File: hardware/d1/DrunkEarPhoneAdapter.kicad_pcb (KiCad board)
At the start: 4 copper layers, 50 x 35 mm, 185 parts, among them J3 SWD, J4 UART, Q1 CSD17577Q3A, Q2 CSD17577Q3A, Q3 DMG1012T-7, SW1 SSSS811101, SW2 DSHP04TS-S, U1 CS43131-CNZR, U10 BLM15PX601SN1D, U11 TPS7A2033PDBVR, U12 TPS7A2018PDBVR, U13 TPS7A2018PDBVR, U14 BLM15PX601SN1D, U15 ESDA25P35-1U1M, U16 ESDA25P35-1U1M, U17 SN74LVC1G32DBVR, U18 TPS22917DBVR, U19 TPS22917DBVR, U2 STM32G0B1VCT6, U20 SN74AVC4T774RSVR, U21 TCA9406DCUR, U3 TS3USB221RSER, U4 TCPP03-M20, U5 TCPP03-M20, U6 ES8327, U7 TPS7A2018PDBVR, U8 TPS7A2033PDBVR, U9 TPS560430XFDBVR, X1 22.5792MHz, X3 24.576MHz

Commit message: Fix Caps
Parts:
- removed C53, C55: 4.7uF 10V X5R, JLCImport:CL05A475MP5NRNC
- added C2: 4.7uF 10V X5R, Capacitor_SMD:C_0603_1608Metric, F.Cu at (66.9, 124.2)
- added C3: 4.7uF 10V X5R, Capacitor_SMD:C_0603_1608Metric, F.Cu at (60.5, 130.9)
- added C85: 1uF 25V X5R, JLCImport:CL05A105KA5NQNC, F.Cu at (70.3, 124.0)
- added JP2: SolderJumper_2_Bridged, Jumper:SolderJumper-2_P1.3mm_Bridged_RoundedPad1.0x1.5mm, F.Cu at (60.7, 118.8)
- added JP3: SolderJumper_2_Bridged, Jumper:SolderJumper-2_P1.3mm_Bridged_RoundedPad1.0x1.5mm, F.Cu at (60.7, 122.3)
- added JP4: SolderJumper_2_Bridged, Jumper:SolderJumper-2_P1.3mm_Bridged_RoundedPad1.0x1.5mm, F.Cu at (60.7, 125.9)
- added R43: 100kΩ, JLCImport:0402WGF1003TCE, F.Cu at (70.4, 128.5)
- C16, C7: footprint JLCImport:CL05A475MP5NRNC -> Capacitor_SMD:C_0603_1608Metric
- C31, C32: value 2.2uF 16V X5R -> 2.2uF 50V X7R; footprint JLCImport:CL05A225KO5NQNC -> JLCImport:CC0805KKX7R9BB225
- moved C7 58.0 mm to (66.9, 128.7)
- moved C16 47.8 mm to (66.9, 131.2)
- moved C31 16.3 mm to (67.4, 118.5)
- moved C32 16.2 mm to (67.4, 121.4)
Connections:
- C16 pad 1: Net-(U1-VP) -> GND
- C16 pad 2: GND -> +3V3_D
- C32 pad 1: GND -> /dac/VCP_FILT-
- C32 pad 2: /dac/VCP_FILT- -> GND
- C66 pad 1: /ucpd/GDPs -> /ucpd/USB_PHONE_ISENSE
- C7 pad 2: +1V8_D -> +3V3_D
- U4 pad 8: unconnected-(U4-GDCs-Pad8) -> /ucpd/GDCs
- U5 pad 6: unconnected-(U5-GDPs-Pad6) -> /ucpd/GDPs_CHR
- U5 pad 8: unconnected-(U5-GDCs-Pad8) -> /ucpd/GDCs_CHR

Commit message: Fixes
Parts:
- removed R43: 100kΩ, JLCImport:0402WGF1003TCE
- added R26: 47kΩ, Resistor_SMD:R_0402_1005Metric, F.Cu at (45.5, 61.5)
- R19, R20: value 510Ω -> 549Ω
- moved R19 25.6 mm to (40.0, 61.8)
- moved R20 25.6 mm to (40.0, 64.3)
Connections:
- R42 pad 2: /ucpd/USB_DIR -> /mcu/USB_DIR
- SW1 pad 1: GND -> unconnected-(SW1-Pad1)
- U3 pad 9: /ucpd/USB_DIR -> /mcu/USB_DIR

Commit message: Replace parts
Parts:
- removed C34: 2.2uF 16V X5R, JLCImport:CL05A225KO5NQNC
- removed C44, C50, C52: 100nF 16V X7R, JLCImport:CL05B104KO5NNNC
- removed C70, C71, C72, C73: 330pF 50V, Capacitor_SMD:C_0402_1005Metric
- removed C80, C81, C82, C83: 1nF 50V X7R, Capacitor_SMD:C_0402_1005Metric
- removed R40, R41: 10kΩ 0603, Resistor_SMD:R_0603_1608Metric
- added C100: 100nF 50V, Capacitor_SMD:C_0402_1005Metric, F.Cu at (46.6, 162.4)
- added C101: 100nF 50V, Capacitor_SMD:C_0402_1005Metric, F.Cu at (41.7, 135.0)
- added C102: 100nF 50V, Capacitor_SMD:C_0402_1005Metric, F.Cu at (41.7, 137.0)
- added C103: 100nF 50V, Capacitor_SMD:C_0402_1005Metric, F.Cu at (41.7, 138.9)
- added C104: 100nF 50V, Capacitor_SMD:C_0402_1005Metric, F.Cu at (41.7, 140.9)
- added C105: 100nF 50V, Capacitor_SMD:C_0402_1005Metric, F.Cu at (31.9, 160.7)
- added C106: 100nF 50V, Capacitor_SMD:C_0402_1005Metric, F.Cu at (46.6, 164.4)
- added C53: 100nF 50V, Capacitor_SMD:C_0402_1005Metric, F.Cu at (35.9, 135.0)
- added C55: 100nF 50V, Capacitor_SMD:C_0402_1005Metric, F.Cu at (35.9, 137.0)
- added C95: 100nF 50V, Capacitor_SMD:C_0402_1005Metric, F.Cu at (31.9, 154.8)
- added C96: 100nF 50V, Capacitor_SMD:C_0402_1005Metric, F.Cu at (31.9, 156.8)
- added C97: 100nF 50V, Capacitor_SMD:C_0402_1005Metric, F.Cu at (46.6, 160.5)
- added C98: 100nF 50V, Capacitor_SMD:C_0402_1005Metric, F.Cu at (38.8, 140.9)
- added C99: 100nF 50V, Capacitor_SMD:C_0402_1005Metric, F.Cu at (31.9, 158.8)
- added R27: 33Ω, Resistor_SMD:R_0402_1005Metric, F.Cu at (36.0, 144.9)
- added R43: 33Ω, Resistor_SMD:R_0402_1005Metric, F.Cu at (36.0, 148.8)
- added R44: 33Ω, Resistor_SMD:R_0402_1005Metric, F.Cu at (36.0, 150.8)
- C1, C19, C20, C21, C22: value 100nF 16V X7R -> 1nF 50V; footprint JLCImport:CL05B104KO5NNNC -> Capacitor_SMD:C_0402_1005Metric
- C13: value 4.7uF 10V X5R -> 2.2uF 16V; footprint JLCImport:CL05A475MP5NRNC -> Capacitor_SMD:C_0603_1608Metric
- C16, C2, C3, C7: value 4.7uF 10V X5R -> 2.2uF 16V
- C23, C24, C35, C37, C39, C40: value 100nF 16V X7R -> 4.7uF 16V; footprint JLCImport:CL05B104KO5NNNC -> Capacitor_SMD:C_0603_1608Metric
- C25: value 2.2uF 16V X5R -> 2.2uF 16V; footprint JLCImport:CL05A225KO5NQNC -> Capacitor_SMD:C_0603_1608Metric
- C26, C27: value 15uF 35V X5R -> 22uF 25V X5R; footprint JLCImport:C2012X5R1V156MT000E -> JLCImport:CL21A226MAQNNNE
- C28, C29, C30, C33: value 2.2uF 16V X5R -> 330pF 50V; footprint JLCImport:CL05A225KO5NQNC -> Capacitor_SMD:C_0603_1608Metric
- C54, C56, C69, C74, C77, C78, C79, C84, C89, C90, C91, C92: value 100nF 16V X7R -> 100nF 50V; footprint JLCImport:CL05B104KO5NNNC -> Capacitor_SMD:C_0402_1005Metric
- C86, C87, C88: value 100nF 50V X7R -> 100nF 50V
- R16, R9: value 33Ω -> 1kΩ
- R23: value 0Ω -> 1kΩ
- R30: value 0Ω -> 10kΩ; footprint Resistor_SMD:R_0402_1005Metric -> Resistor_SMD:R_0603_1608Metric
- R35: value 1kΩ -> 10kΩ; footprint Resistor_SMD:R_0402_1005Metric -> Resistor_SMD:R_0603_1608Metric
- moved R38 154.6 mm to (36.0, 146.9)
- moved R16 147.1 mm to (50.6, 146.8)
- moved C69 144.7 mm to (46.6, 158.5)
- moved C56 123.3 mm to (46.6, 156.5)
- moved C35 93.2 mm to (37.4, 155.1)
- moved C40 93.0 mm to (37.4, 157.6)
- moved C39 89.4 mm to (50.0, 157.3)
- moved C86 84.9 mm to (40.8, 156.8)
- moved C37 84.1 mm to (50.0, 154.8)
- moved C87 69.0 mm to (53.4, 140.9)
- moved C88 69.0 mm to (53.4, 142.9)
- moved C89 67.9 mm to (35.9, 140.9)
- moved C13 67.6 mm to (32.5, 142.8)
- moved C84 67.2 mm to (53.4, 138.9)
- moved C90 62.6 mm to (38.8, 135.0)
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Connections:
- C1 pad 1: Net-(U9-CB) -> unconnected-(C1-Pad1)
- C1 pad 2: Net-(U9-SW) -> unconnected-(C1-Pad2)
- C13 pad 1: GND -> +1V8_CP
- C13 pad 2: +1V8_CP -> GND
- C16 pad 1: GND -> /dac/FLYP_VCP
- C16 pad 2: +3V3_D -> /dac/FLYC_VCP
- C19 pad 1: Net-(U18-QOD) -> GND
- C19 pad 2: GND -> /mcu/ADC1_IN0
- C2 pad 2: Net-(U1-VP) -> +1V8_A
- C20 pad 1: Net-(U2-VREF+) -> GND
- C20 pad 2: GND -> /mcu/ADC1_IN1
- C21 pad 2: Net-(U1-VP) -> /mcu/ADC1_IN2
- C22 pad 1: Net-(U1-VD) -> GND
- C22 pad 2: GND -> /mcu/ADC1_IN3
- C23 pad 1: GND -> unconnected-(C23-Pad1)
- C23 pad 2: +1V8_A -> unconnected-(C23-Pad2)
- C24 pad 1: Net-(U1-VD) -> GND
- C24 pad 2: GND -> Net-(U1-VP)
- C25 pad 1: +1V8_A -> /dac/FLYC_VCP
- C25 pad 2: GND -> /dac/FLYN_VCP
- C27 pad 1: /dac/-VA -> /dac/FILT-
- C27 pad 2: /dac/FILT- -> /dac/-VA
- C28 pad 1: /dac/-VA -> GND
- C28 pad 2: GND -> /ucpd/USB_CHR_CC1
- C29 pad 1: /dac/FLYP_VA -> GND
- C29 pad 2: /dac/FLYN_VA -> /ucpd/USB_CHR_CC2
- C3 pad 1: GND -> /dac/-VA
- C3 pad 2: +1V8_D -> GND
- C30 pad 1: +1V8_CP -> GND
- C30 pad 2: GND -> /ucpd/USB_PHONE_CC1
- C33 pad 1: /dac/FLYP_VCP -> GND
- C33 pad 2: /dac/FLYC_VCP -> /ucpd/USB_PHONE_CC2
- C35 pad 1: Net-(U6-AVDD) -> GND
- C35 pad 2: GND -> +1V8_D
- C37 pad 1: Net-(U6-CPVDD) -> GND
- C37 pad 2: GND -> +3V3_D
- C39 pad 1: +3V3_D -> GND
- C39 pad 2: GND -> +3V3_D
- C40 pad 1: +3V3_D -> GND
- C40 pad 2: GND -> +1V8_CP
- C54 pad 1: +3V3_D -> GND
- C54 pad 2: GND -> +3V3_D
- C56 pad 1: GND -> /mcu/NRST
- C56 pad 2: /mcu/NRST -> GND
- C69 pad 1: +3V3_D -> GND
- C69 pad 2: GND -> +3V3_D
- C7 pad 1: GND -> /dac/FLYN_VA
- C7 pad 2: +3V3_D -> /dac/FLYP_VA
- C74 pad 1: +3V3_D -> GND
- C74 pad 2: GND -> +3V3_D
- C78 pad 1: Net-(U17-VCC) -> GND
- C78 pad 2: GND -> +3V3_D
- C79 pad 1: Net-(U17-VCC) -> Net-(U9-CB)
- C79 pad 2: GND -> Net-(U9-SW)
- C84 pad 1: +3V3_D -> GND
- C84 pad 2: GND -> +3V3_D
- C88 pad 1: GND -> Net-(U5-CBIAS)
- C88 pad 2: Net-(U5-CBIAS) -> GND
- C89 pad 1: GND -> +1V8_D
- C89 pad 2: +1V8_D -> GND
- C90 pad 1: +3V3_D -> GND
- C90 pad 2: GND -> +3V3_D
- C91 pad 1: GND -> +3V3_D
- C91 pad 2: +3V3_D -> GND
- C92 pad 1: GND -> +1V8_D
- C92 pad 2: +1V8_D -> GND
- R16 pad 1: Net-(U17-Y) -> /mcu/ADC1_IN2
- R16 pad 2: Net-(U1-XTI/MCLK) -> Net-(U5-IANA)
- R23 pad 1: /mcu/ADC1_IN0 -> Net-(U1-HP_DETECT)
- R23 pad 2: Net-(U4-IANA) -> /dac/JACK_TIP_DETECT
- R30 pad 1: /mcu/ADC1_IN2 -> /ucpd/VSENSE_PHONE
- R30 pad 2: Net-(U5-IANA) -> /ucpd/USB_PHONE_VBUS
- R35 pad 1: Net-(U1-HP_DETECT) -> /ucpd/VSENSE_CHR
- R35 pad 2: /dac/JACK_TIP_DETECT -> /ucpd/USB_CHR_VBUS
- R9 pad 1: Net-(U20-B3) -> /mcu/ADC1_IN0
- R9 pad 2: /adc/CLKIN -> Net-(U4-IANA)

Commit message: Trace
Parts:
- removed C1: 1nF 50V, Capacitor_SMD:C_0402_1005Metric
- removed C23: 4.7uF 16V, Capacitor_SMD:C_0603_1608Metric
- removed NT1: NetTie_2, NetTie:NetTie-2_SMD_Pad0.5mm
- removed R17: 10mΩ 500mW, Resistor_SMD:R_0805_2012Metric
- removed USBC2: ~, JLCImport:USBC_EXT_5P
- added NT3: NetTie_3, NetTie:NetTie-3_SMD_Pad0.5mm, F.Cu at (63.2, 44.7)
- added USBC3: ~, JLCImport:USBC_EXT_5P, F.Cu at (44.9, 36.7)
- added USBC4: ~, JLCImport:USBC_EXT_5P, B.Cu at (44.9, 36.7)
- C101, C102, C103, C104, C13, C2, C24, C85, L3, R23: moved to B.Cu
- R27: value 33Ω -> 7mΩ 500mW; footprint Resistor_SMD:R_0402_1005Metric -> Resistor_SMD:R_0805_2012Metric
- moved C40 227.3 mm to (252.1, 82.9)
- moved D2 224.6 mm to (272.3, 135.2)
- moved R1 224.6 mm to (270.4, 148.6)
- moved C51 221.8 mm to (265.7, 132.9)
- moved C57 221.8 mm to (265.7, 136.3)
- moved C58 221.8 mm to (265.7, 139.7)
- moved C59 221.8 mm to (265.7, 143.0)
- moved C60 221.8 mm to (265.7, 146.3)
- moved C9 221.8 mm to (265.7, 129.6)
- moved C15 204.0 mm to (252.1, 76.9)
- moved U13 204.0 mm to (256.5, 85.9)
- moved U7 199.5 mm to (223.6, 79.5)
- moved C35 197.0 mm to (221.7, 85.5)
- moved TP3 191.6 mm to (256.6, 78.7)
- moved C14 177.3 mm to (225.4, 82.9)
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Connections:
- Audio1 pad 4: GND -> /headset/JACK_RING_2
- D4 pad 4: /dac/JACK_TIP_DETECT -> /adc/GMS1
- D4 pad 5: /adc/GMS1 -> /dac/JACK_TIP_DETECT
- L7 pad 5: Net-(USBC2-D-) -> /ucpd/D_P
- L7 pad 6: Net-(USBC2-D+) -> /ucpd/D_N
- NT2 pad 2: GND -> /headset/JACK_RING_2
- R27 pad 1: unconnected-(R27-Pad1) -> /ucpd/USB_CHR_VBUS
- R27 pad 2: unconnected-(R27-Pad2) -> /ucpd/USB_CHR_ISENSE
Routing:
- net GND: track 0.00 -> 33.8 mm, vias 0 -> 145
- net /adc/GMS1: track 0.00 -> 29.7 mm, vias 0 -> 2
- net /adc/GMS0: track 0.00 -> 28.2 mm
- net /dac/HPREFA: track 0.00 -> 18.3 mm
- net +3V8: track 0.00 -> 15.6 mm, vias 0 -> 36
- net /adc/MIC1P: track 0.00 -> 13.1 mm, vias 0 -> 2
- net /dac/JACK_TIP_DETECT: track 0.00 -> 12.6 mm, vias 0 -> 1
- net /dac/JACK_RING_1: track 0.00 -> 11.8 mm
- net /dac/FLYN_VCP: track 0.00 -> 11.7 mm
- net /dac/JACK_TIP: track 0.00 -> 10.9 mm
- net /adc/MIC1N: track 0.00 -> 10.9 mm, vias 0 -> 2
- net /dac/HPREFB: track 0.00 -> 10.0 mm
- net /ucpd/USB_CHR_DP: track 0.00 -> 9.03 mm, vias 0 -> 2
- net /ucpd/USB_CHR_DN: track 0.00 -> 8.58 mm, vias 0 -> 2
- net /ucpd/USB_CHR_VBUS: track 0.00 -> 7.59 mm, vias 0 -> 4
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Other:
- board size 50 x 35 mm -> 50 x 45 mm

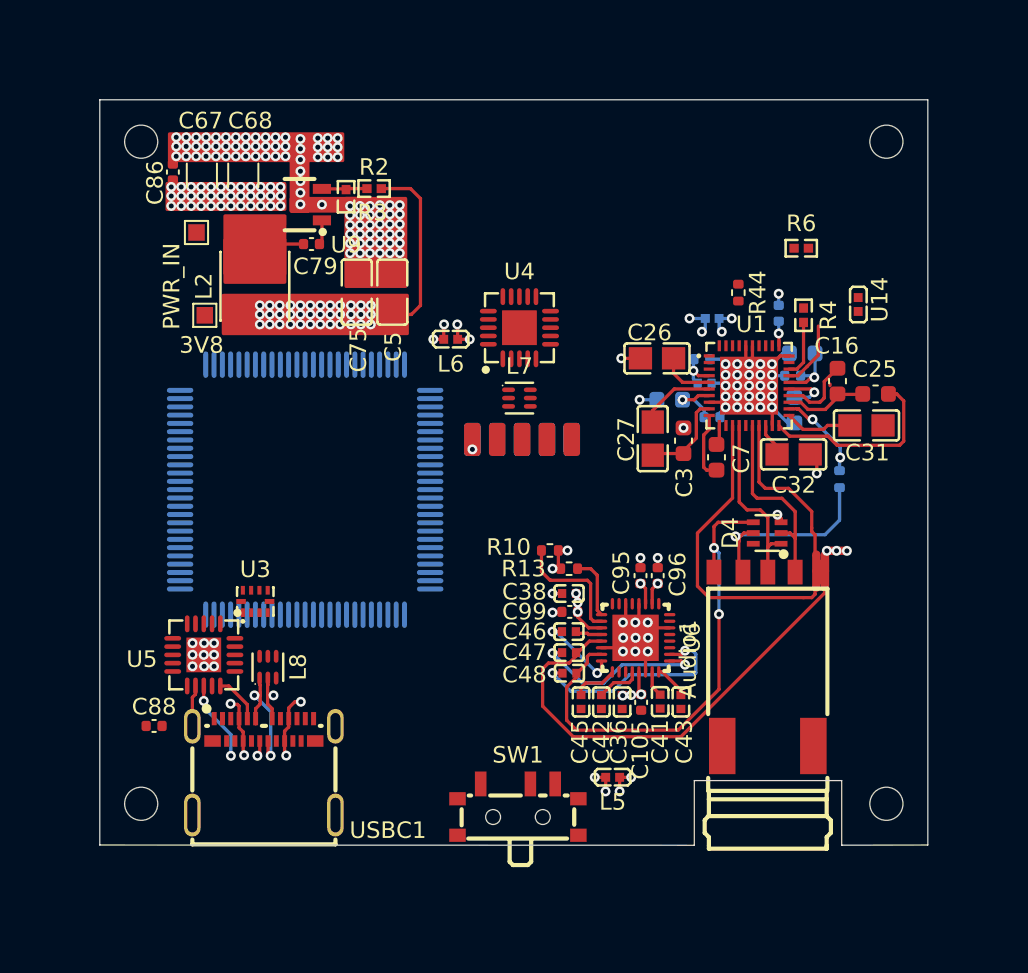
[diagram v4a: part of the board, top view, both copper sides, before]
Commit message: Replace USB
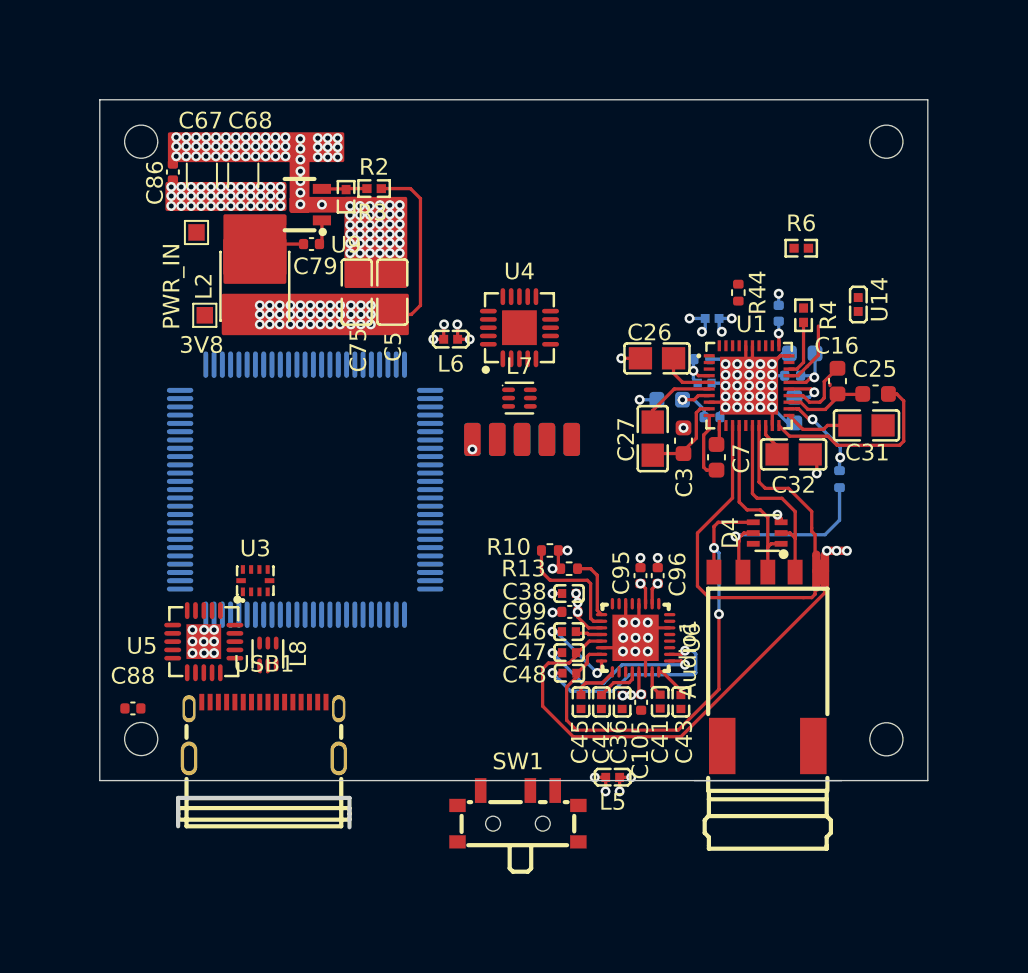
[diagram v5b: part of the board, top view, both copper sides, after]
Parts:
- removed USBC1: 105450-0101, JLCImport:105450-0101
- added USB1: 2130830005, JLCImport:2130830005, F.Cu at (29.3, 54.3)
- moved C88 1.66 mm to (21.4, 53.0)
- moved U3 1.25 mm to (28.8, 45.3)
- moved L8 0.80 mm to (29.6, 49.7)
- moved U5 0.80 mm to (25.7, 49.0)
- moved SW1 0.40 mm to (44.7, 59.5)
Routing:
- net /ucpd/USB_CHR_DP: track 9.03 -> 0.43 mm, vias 2 -> 0
- net /ucpd/USB_CHR_DN: track 8.58 -> 0.43 mm, vias 2 -> 0
- net /ucpd/USB_CHR_VBUS: track 7.59 -> 0.00 mm, vias 4 -> 0
- net /ucpd/USB_CHR_CC2: track 4.90 -> 0.00 mm, vias 2 -> 0
- net /ucpd/USB_CHR_CC1: track 2.94 -> 0.00 mm
- net GND: track 33.8 -> 31.3 mm
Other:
- board size 50 x 45 mm -> 50 x 41.1 mm

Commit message: Fix layout
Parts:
- USB1: value 2130830005 -> ~
- moved USB1 0.11 mm to (29.3, 54.2)
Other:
- outline, holes or cut-outs redrawn
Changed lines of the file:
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@@
 	(footprint "JLCImport:2130830005"
 		(layer "F.Cu")
-		(at 29.32 54.30661)
+		(at 29.3 54.2)
 		(descr "-40℃~+85℃ 1 10000 times 16P 30V 5A Black Female Type-C USB 2.0 SMD USB Connectors ROHS")
 		(tags "2130830005 C2839029 MOLEX USB-SMD_16P-P0.50_2130830005")
@@
 			)
 		)
-		(property "Value" "2130830005"
+		(property "Value" "~"
 			(at 0 6.86 0)
 			(layer "F.Fab")
@@
 		(sheetname "/ucpd/")
 		(sheetfile "ucpd.kicad_sch")
-		(units
-			(unit
-				(name "A")
-				(pins "A1" "A4" "A5" "A6" "A7" "A8" "A9" "A12" "20" "17" "19" "18" "B12"
-					"B9" "B8" "B7" "B6" "B5" "B4" "B1"
-				)
-			)
-		)
 		(attr through_hole)
 		(duplicate_pad_numbers_are_jumpers no)
@@
 				(type solid)
 			)
-			(layer "Edge.Cuts")
+			(layer "Cmts.User")
 		)
 		(fp_line
@@
 				(type solid)
 			)
-			(layer "Edge.Cuts")
+			(layer "Cmts.User")
 		)
 		(fp_line
@@
 				(type solid)
 			)
-			(layer "Edge.Cuts")
+			(layer "Cmts.User")
 		)
 		(fp_line
@@
 				(type solid)
 			)
-			(layer "Edge.Cuts")
+			(layer "Cmts.User")
 		)
 		(fp_poly
@@
 		(net "GND")
 	)
-	(gr_line
-		(start 19.41 16.236749)
-		(end 19.41 57.346749)
-		(stroke
-			(width 0.05)
-			(type default)
-		)
-		(layer "Edge.Cuts")
-	)
-	(gr_line
-		(start 19.41 16.236749)
-		(end 69.41 16.236749)
-		(stroke
-			(width 0.05)
-			(type default)
-		)
-		(layer "Edge.Cuts")
-	)
-	(gr_line
-		(start 19.41 57.346749)
-		(end 69.41 57.346749)
+	(gr_rect
+		(start 19.4 16.2)
+		(end 69.4 57.3)
 		(stroke
-			(width 0.05)
+			(width 0.1)
 			(type default)
 		)
+		(fill no)
 		(layer "Edge.Cuts")
 	)
@@
 		(layer "Edge.Cuts")
 	)
-	(gr_line
-		(start 69.41 57.346749)
-		(end 69.41 16.236749)
-		(stroke
-			(width 0.05)
-			(type default)
-		)
-		(layer "Edge.Cuts")
-	)
 	(segment
 		(start 60.326863 41.292859)
@@
 	)
 	(segment
-		(start 29.095127 50.776749)
-		(end 29.06 50.741622)
-		(width 0.2)
-		(layer "F.Cu")
-		(net "/ucpd/USB_CHR_DP")
-	)
-	(segment
-		(start 29.06 50.741622)
-		(end 29.06 50.357606)
-		(width 0.2)
-		(layer "F.Cu")
-		(net "/ucpd/USB_CHR_DP")
-	)
-	(segment
-		(start 29.545127 50.776749)
-		(end 29.559873 50.762003)
-		(width 0.2)
-		(layer "F.Cu")
-		(net "/ucpd/USB_CHR_DN")
-	)
-	(segment
-		(start 29.559873 50.762003)
-		(end 29.559873 50.357606)
-		(width 0.2)
-		(layer "F.Cu")
-		(net "/ucpd/USB_CHR_DN")
-	)
-	(segment
 		(start 47.35 50.86)
 		(end 46.71 50.86)
@@
 	)
 	(segment
+		(start 29.095127 50.776749)
+		(end 29.06 50.741622)
+		(width 0.2)
+		(layer "F.Cu")
+		(net "/ucpd/USB_CHR_DP")
+	)
+	(segment
+		(start 29.06 50.741622)
+		(end 29.06 50.357606)
+		(width 0.2)
+		(layer "F.Cu")
+		(net "/ucpd/USB_CHR_DP")
+	)
+	(segment
+		(start 29.545127 50.776749)
+		(end 29.559873 50.762003)
+		(width 0.2)
+		(layer "F.Cu")
+		(net "/ucpd/USB_CHR_DN")
+	)
+	(segment
+		(start 29.559873 50.762003)
+		(end 29.559873 50.357606)
+		(width 0.2)
+		(layer "F.Cu")
+		(net "/ucpd/USB_CHR_DN")
+	)
+	(segment

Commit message: Traces
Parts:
- C64, C88, U15, U16, U17, U18, U19, X1, X3: moved to B.Cu
- USB1: value ~ -> 2130830005
- moved U13 220.8 mm to (44.7, 23.4), turned to -90 degrees
- moved C15 216.7 mm to (42.2, 22.9), turned to 90 degrees
- moved TP3 215.0 mm to (49.4, 21.6)
- moved C40 213.2 mm to (47.5, 22.9), turned to 90 degrees
- moved U10 196.2 mm to (53.4, 21.9)
- moved C14 191.2 mm to (42.2, 28.5), turned to 90 degrees
- moved TP2 187.5 mm to (49.4, 27.3)
- moved U7 185.8 mm to (44.7, 28.9), turned to -90 degrees
- moved U12 185.0 mm to (57.6, 23.9), turned to -90 degrees
- moved C35 183.3 mm to (47.5, 28.4), turned to 90 degrees
- moved C12 182.8 mm to (55.1, 23.4), turned to 90 degrees
- moved TP4 182.1 mm to (61.8, 22.1)
- moved C11 177.3 mm to (60.1, 23.5), turned to 90 degrees
- moved TP5 170.8 mm to (49.6, 32.9)
- moved C10 170.7 mm to (42.2, 34.0), turned to 90 degrees
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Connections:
- U11 pad 4: unconnected-(U11-NC-Pad4) -> GND
- U12 pad 4: unconnected-(U12-N/C-Pad4) -> GND
- U13 pad 4: unconnected-(U13-N/C-Pad4) -> GND
- U7 pad 4: unconnected-(U7-N/C-Pad4) -> GND
- U8 pad 4: unconnected-(U8-NC-Pad4) -> GND
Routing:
- net Net-(U17-Y): track 0.00 -> 31.5 mm, vias 0 -> 1
- net /mcu/USB_DN: track 0.00 -> 29.9 mm, vias 0 -> 1
- net /mcu/USB_DP: track 0.00 -> 28.4 mm, vias 0 -> 1
- net GND: track 31.3 -> 55.2 mm, vias 145 -> 218
- net /ucpd/USB_PHONE_SAFE_DP: track 0.00 -> 18.4 mm
- net /ucpd/USB_PHONE_SAFE_DN: track 0.00 -> 16.9 mm
- net /ucpd/USB_PHONE_VBUS: track 0.00 -> 15.0 mm, vias 0 -> 6
- net /ucpd/USB_CHR_CC2: track 0.00 -> 14.8 mm
- net /ucpd/USB_CHR_VBUS: track 0.00 -> 13.6 mm, vias 0 -> 11
- net /ucpd/USB_CHR_SAFE_DN: track 0.00 -> 9.93 mm
- net /ucpd/USB_CHR_SAFE_DP: track 0.00 -> 9.93 mm
- net Net-(U19-QOD): track 0.00 -> 7.42 mm
- net Net-(U18-QOD): track 0.00 -> 7.04 mm
- net PWR_IN: track 0.00 -> 5.97 mm, vias 36 -> 42
- net +3V8: track 15.6 -> 21.3 mm, vias 36 -> 76
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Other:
- board size 50 x 41.1 mm -> 50 x 50 mm
